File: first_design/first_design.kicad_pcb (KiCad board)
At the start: 2 copper layers, 66 x 57 mm, 0 parts

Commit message: working on PCB design
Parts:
- added 2N7002K1: NMOS_DGS, library_express_pro:SOT23, F.Cu at (147.0, 60.0)
- added 2N7002K2: NMOS_DGS, library_express_pro:SOT23, F.Cu at (159.5, 47.4)
- added AI-1223-TWT-5V-5-R1: Buzzer, library_express_pro:Buzzer_AI-1223-TWT-5V-5-R, F.Cu at (156.5, 32.4)
- added C1: 10uF, library_express_pro:RLC_EIA_3216, F.Cu at (112.0, 62.0)
- added C2: 170uF, library_express_pro:RLC_EIA_3216, F.Cu at (105.7, 62.1)
- added C3: 100nF, library_express_pro:RLC_EIA_3216, F.Cu at (122.3, 48.2)
- added C4: 1uF, library_express_pro:RLC_EIA_3216, F.Cu at (72.0, 70.0)
- added C5: 1uF, library_express_pro:RLC_EIA_3216, F.Cu at (72.0, 75.0)
- added C6: 0.1uF, library_express_pro:RLC_EIA_3216, F.Cu at (60.0, 75.0)
- added C7: 44uF, library_express_pro:RLC_EIA_3216, F.Cu at (66.0, 70.0)
- added C8: 10uF, library_express_pro:RLC_EIA_3216, F.Cu at (106.4, 49.5)
- added C9: 44uF, library_express_pro:RLC_EIA_3216, F.Cu at (61.0, 69.0)
- added J1: Conn_02x20_Odd_Even, library_express_pro:RaspberryPi_pins, F.Cu at (32.8, 27.0)
- added J2: Accelerometer_small, library_express_pro:accelerometer_small, F.Cu at (141.8, 35.2)
- added J3: Accelerometer_standard, library_express_pro:Accelerometer_standard, F.Cu at (100.9, 45.0)
- added J4: Servo_motor, library_express_pro:servo_connector, F.Cu at (114.2, 45.0)
- added L1: 3.3uH, library_express_pro:RLC_EIA_3216, F.Cu at (56.0, 70.0)
- added LDO1: AZ2085, library_express_pro:TO252-2, F.Cu at (135.4, 39.7)
- added MotorConnector1: Conn_01x02, library_express_pro:Connector_pads, F.Cu at (29.0, 72.0)
- added MotorController1: VNH7070BAS, library_express_pro:SO-16N, F.Cu at (41.6, 74.4)
- added None1: IR_LED, library_express_pro:LED_YSL-R531R3D-D2, F.Cu at (143.1, 54.6)
- added Power1: Conn_01x02, library_express_pro:Connector_pads, F.Cu at (85.0, 65.0)
- added R1: 220, library_express_pro:RLC_EIA_3216, F.Cu at (118.8, 52.0)
- added R10: 220, library_express_pro:RLC_EIA_3216, F.Cu at (137.3, 52.0)
- added R11: 82, library_express_pro:RLC_EIA_3216, F.Cu at (131.1, 55.7)
- added R12: 82, library_express_pro:RLC_EIA_3216, F.Cu at (137.3, 55.7)
- added R13: 82, library_express_pro:RLC_EIA_3216, F.Cu at (124.2, 59.5)
- added R14: 82, library_express_pro:RLC_EIA_3216, F.Cu at (130.4, 59.5)
- added R1_buck1: 124k, library_express_pro:RLC_EIA_3216, F.Cu at (66.0, 66.0)
- added R2: 220, library_express_pro:RLC_EIA_3216, F.Cu at (112.6, 53.2)
- added R2_buck1: 22.1K, library_express_pro:RLC_EIA_3216, F.Cu at (72.0, 66.0)
- added R3: 100K, library_express_pro:RLC_EIA_3216, F.Cu at (118.8, 55.7)
- added R4: 10K, library_express_pro:RLC_EIA_3216, F.Cu at (124.9, 55.7)
- added R5: 10K, library_express_pro:RLC_EIA_3216, F.Cu at (118.1, 59.5)
- added R7: 220, library_express_pro:RLC_EIA_3216, F.Cu at (128.5, 48.2)
- added R8: 220, library_express_pro:RLC_EIA_3216, F.Cu at (134.6, 48.2)
- added R9: 220, library_express_pro:RLC_EIA_3216, F.Cu at (131.1, 52.0)
- added R_IR1: 220, library_express_pro:RLC_EIA_3216, F.Cu at (106.5, 53.0)
- added Rmax1: 280, library_express_pro:RLC_EIA_3216, F.Cu at (88.0, 77.0)
- added Si4101DY1: PMOS, library_express_pro:SOT23, F.Cu at (82.0, 77.0)
- added StepDownConverter1: AP65450, library_express_pro:SO-8, F.Cu at (66.0, 75.0)
- added VoltageMonitor1: BD48K60, library_express_pro:SSOP3, F.Cu at (148.9, 50.7)
- added YSL-R531R3D-D1: LED, library_express_pro:LED_YSL-R531R3D-D2, F.Cu at (154.3, 45.8)
- added YSL-R531R3D-D2: LED, library_express_pro:LED_YSL-R531R3D-D2, F.Cu at (160.5, 42.0)
- added YSL-R531R3D-D3: LED, library_express_pro:LED_YSL-R531R3D-D2, F.Cu at (141.8, 60.4)
- added YSL-R531R3D-D4: LED, library_express_pro:LED_YSL-R531R3D-D2, F.Cu at (136.3, 60.4)

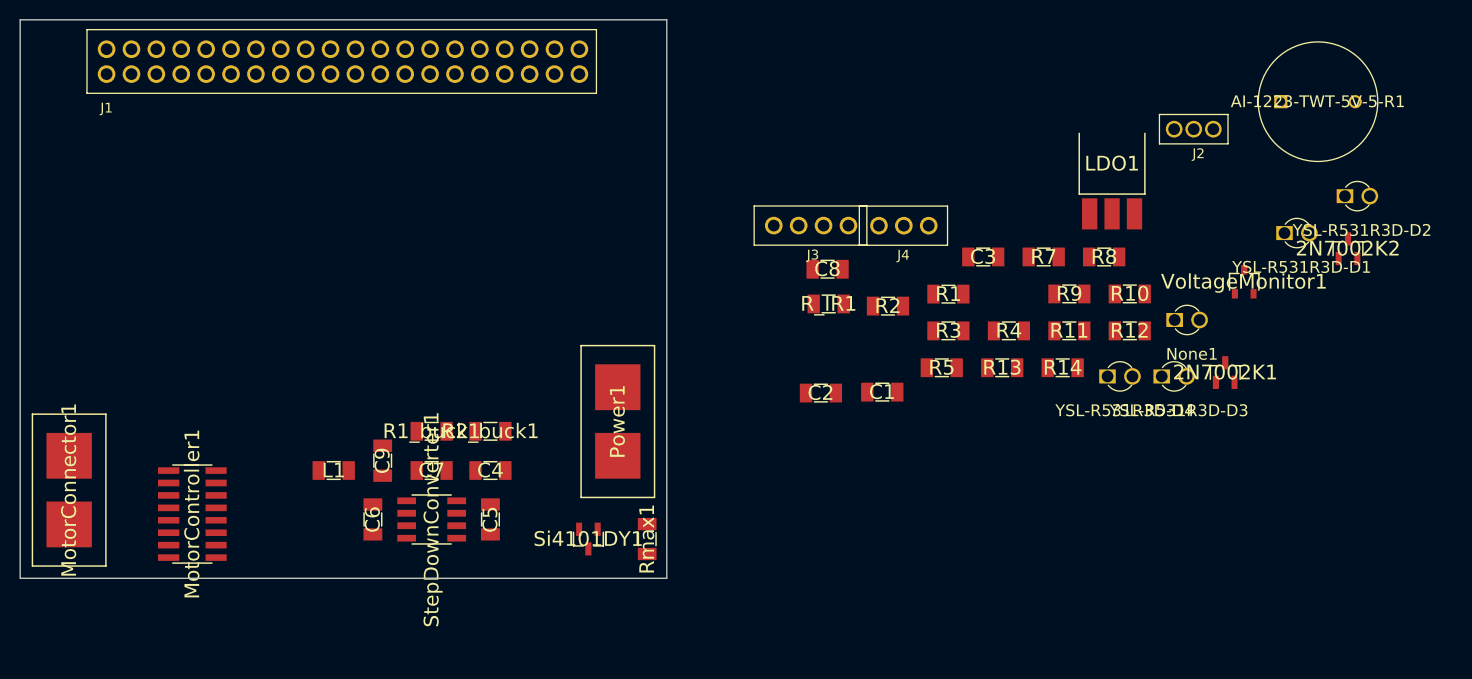
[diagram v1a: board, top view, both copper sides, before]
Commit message: PCB Board first layout
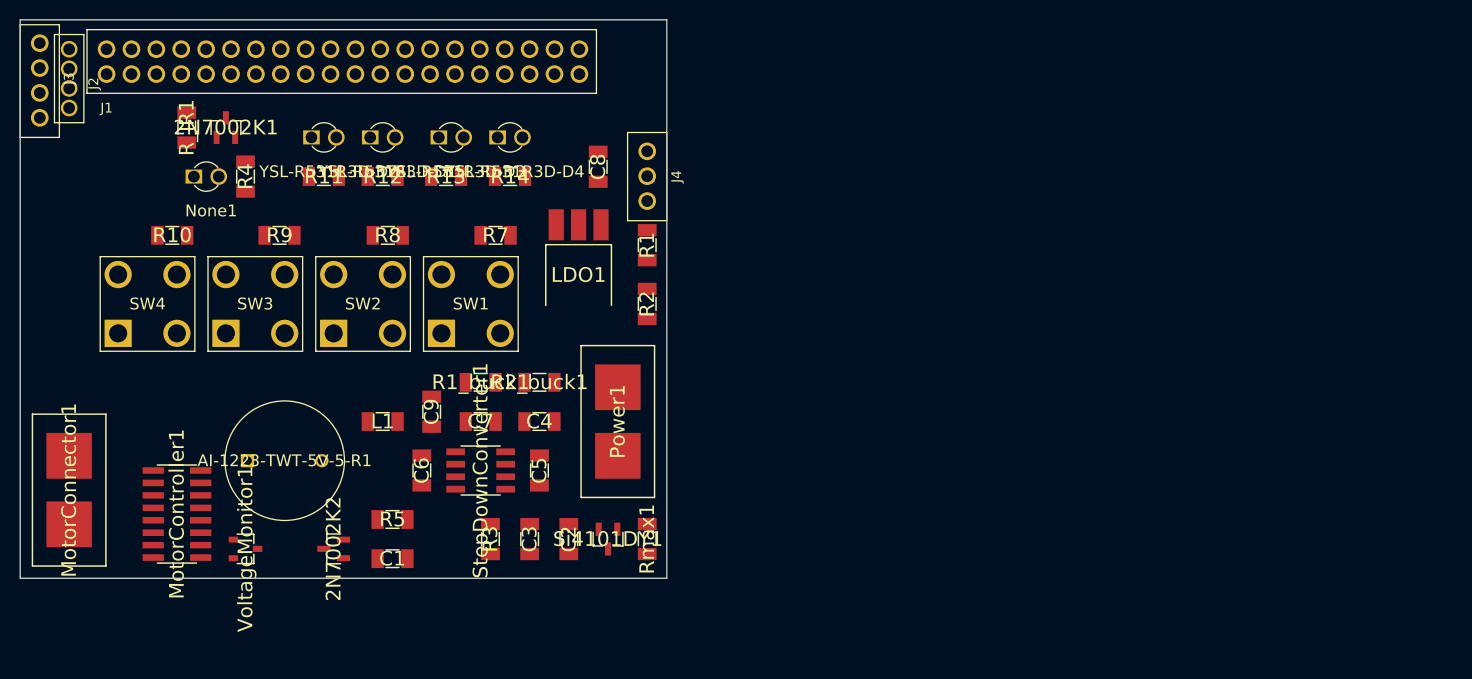
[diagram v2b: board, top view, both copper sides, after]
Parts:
- added SW1: SW_DPST, library_express_pro:button_6x6mm, F.Cu at (67.0, 56.0)
- added SW2: SW_DPST, library_express_pro:button_6x6mm, F.Cu at (56.0, 56.0)
- added SW3: SW_DPST, library_express_pro:button_6x6mm, F.Cu at (45.0, 56.0)
- added SW4: SW_DPST, library_express_pro:button_6x6mm, F.Cu at (34.0, 56.0)
- moved J2 112.8 mm to (29.0, 33.0), turned to 90 degrees
- moved AI-1223-TWT-5V-5-R1 111.7 mm to (51.0, 69.0)
- moved 2N7002K2 108.0 mm to (56.0, 78.0), turned to 90 degrees
- moved YSL-R531R3D-D2 105.7 mm to (55.0, 36.0)
- moved VoltageMonitor1 105.5 mm to (47.0, 78.0), turned to 270 degrees
- moved 2N7002K1 105.0 mm to (45.0, 35.0)
- moved None1 101.2 mm to (43.0, 40.0)
- moved R10 97.9 mm to (39.5, 46.0)
- moved YSL-R531R3D-D1 93.8 mm to (61.0, 36.0)
- moved R9 80.8 mm to (50.5, 46.0)
- moved R4 79.5 mm to (47.0, 40.0), turned to 270 degrees
- moved R12 77.9 mm to (61.0, 40.0)
- moved YSL-R531R3D-D3 77.7 mm to (68.0, 36.0)
- moved R11 77.7 mm to (55.0, 40.0)
- moved J3 75.7 mm to (26.0, 34.0), turned to 90 degrees
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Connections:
- LDO1 pad 1: (no net) -> Net-(LDO1-Pad1)
- LDO1 pad 2: (no net) -> 6V-5V
- LDO1 pad 3: (no net) -> Vbat
- R1 pad 2: Net-(LDO1-Pad~) -> Net-(LDO1-Pad1)
- R2 pad 1: Net-(LDO1-Pad~) -> Net-(LDO1-Pad1)

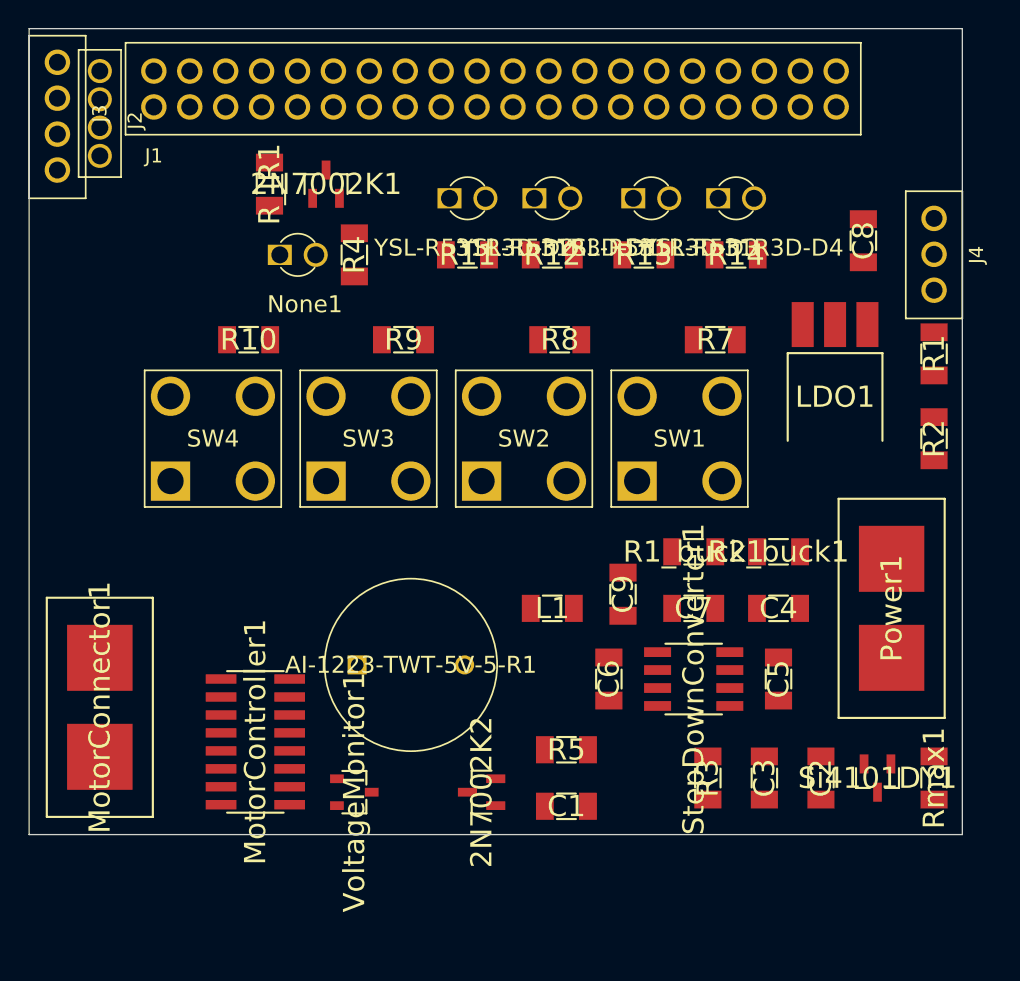
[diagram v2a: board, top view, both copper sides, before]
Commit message: PCB board in the works
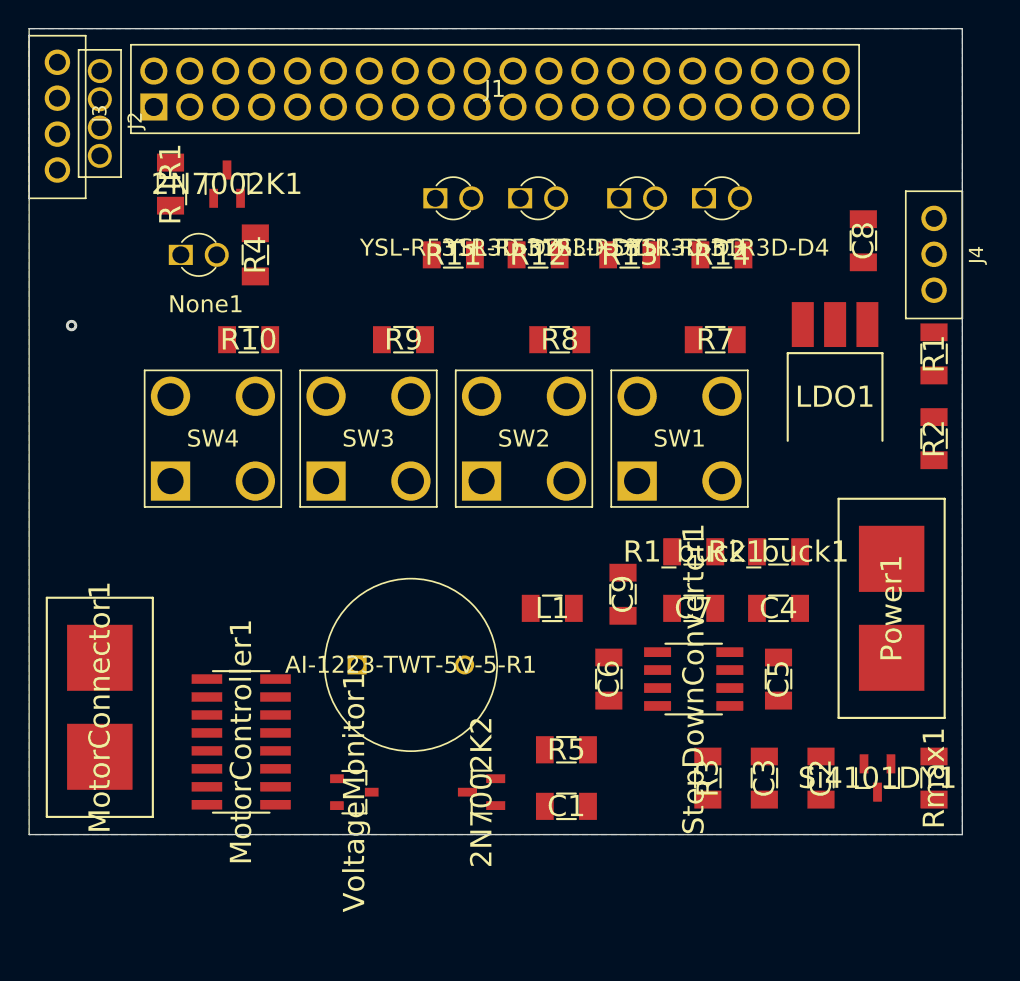
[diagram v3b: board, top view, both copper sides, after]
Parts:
- J1: footprint library_express_pro:RaspberryPi_pins -> library_express_pro:RasPi_header_pro
- moved 2N7002K1 7.00 mm to (38.0, 35.0)
- moved None1 7.00 mm to (36.0, 40.0)
- moved R4 7.00 mm to (40.0, 40.0)
- moved R_IR1 7.00 mm to (34.0, 35.0)
- moved J1 2.54 mm to (32.8, 29.5)
- moved MotorController1 1.00 mm to (39.0, 74.4)
- moved R11 1.00 mm to (54.0, 40.0)
- moved R12 1.00 mm to (60.0, 40.0)
- moved R13 1.00 mm to (66.5, 40.0)
- moved R14 1.00 mm to (73.0, 40.0)
- moved YSL-R531R3D-D1 1.00 mm to (60.0, 36.0)
- moved YSL-R531R3D-D2 1.00 mm to (54.0, 36.0)
- moved YSL-R531R3D-D3 1.00 mm to (67.0, 36.0)
- moved YSL-R531R3D-D4 1.00 mm to (73.0, 36.0)
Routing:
- net GND: vias 0 -> 1
- added copper zone on B.Cu, net GND

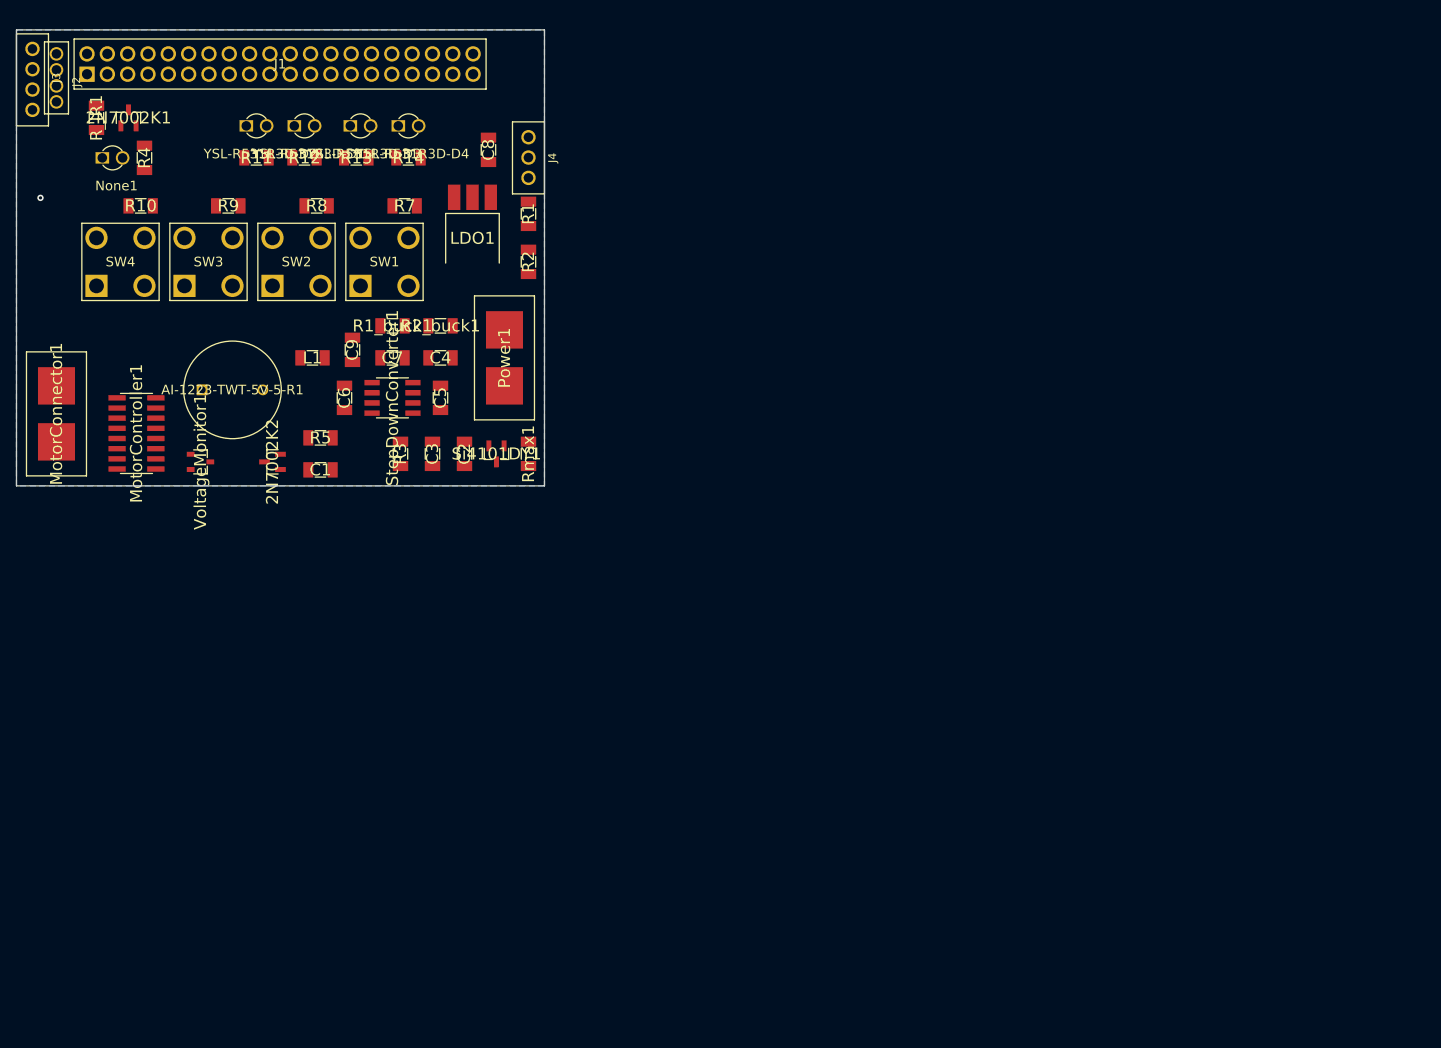
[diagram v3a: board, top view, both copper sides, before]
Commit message: playing with PiHat footprint
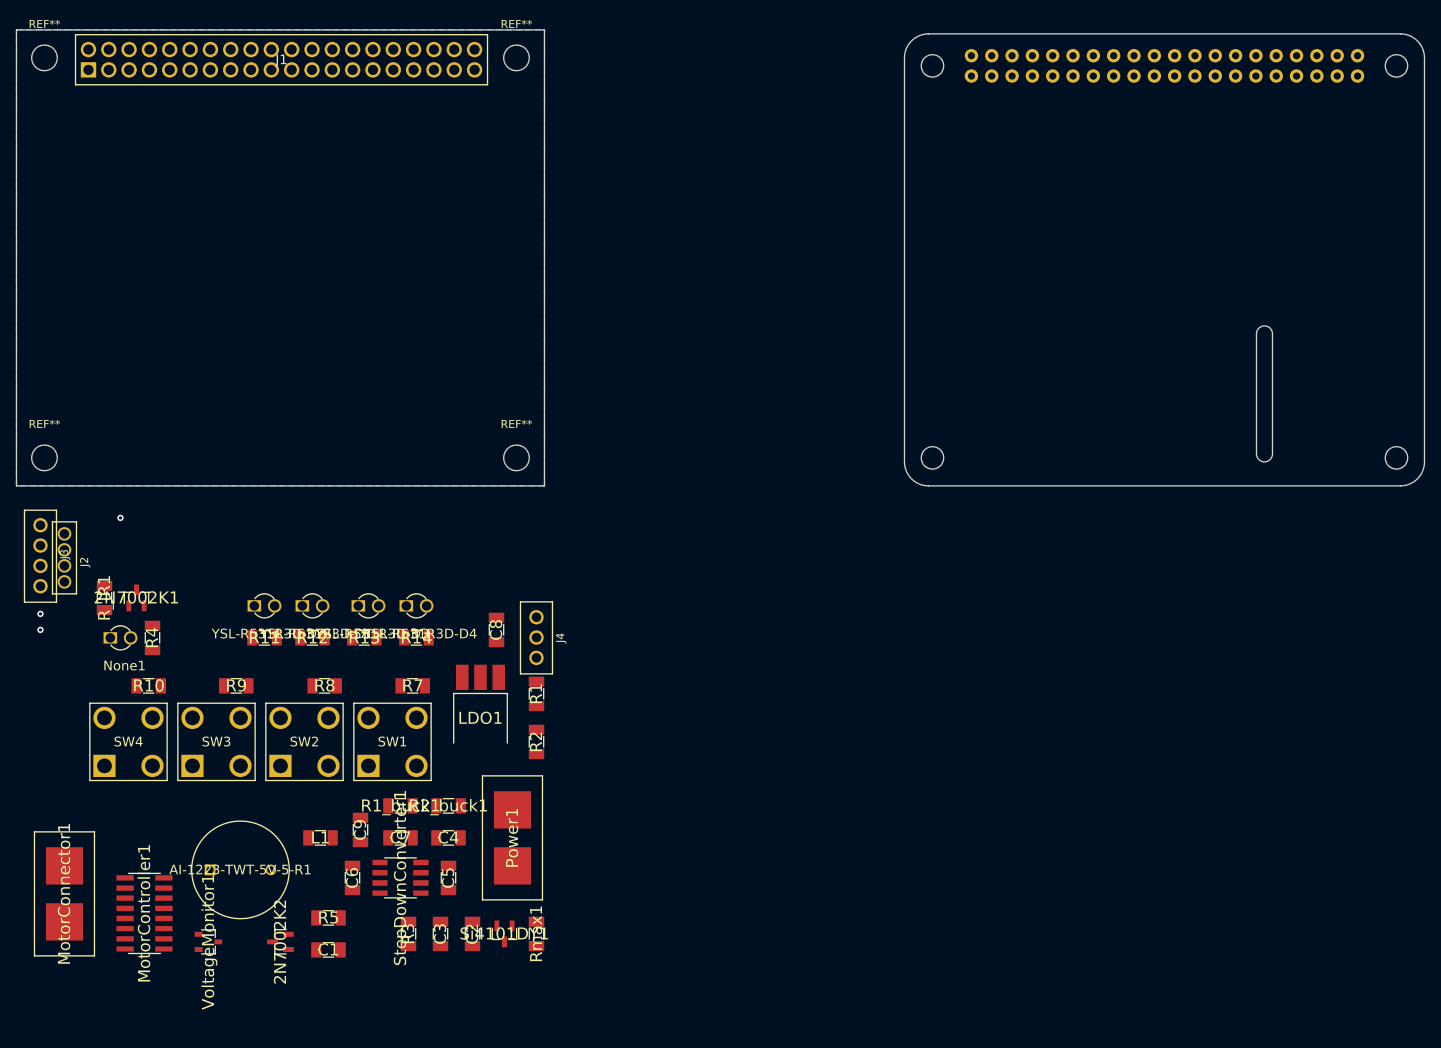
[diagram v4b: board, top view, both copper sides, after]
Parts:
- added REF**: MountingHole_3.2mm_M3, MountingHole:MountingHole_3.2mm_M3, F.Cu at (27.5, 77.5)
- added REF**: MountingHole_3.2mm_M3, MountingHole:MountingHole_3.2mm_M3, F.Cu at (27.5, 27.5)
- added REF**: MountingHole_3.2mm_M3, MountingHole:MountingHole_3.2mm_M3, F.Cu at (86.5, 77.5)
- added REF**: MountingHole_3.2mm_M3, MountingHole:MountingHole_3.2mm_M3, F.Cu at (86.5, 27.5)
- added RPI1: RASPBERRYPI_BPLUS_HATNOSLOTS, Adafruit HaD Proto HAT rev A:PI_HAT_NOSLOTS, F.Cu at (135.0, 81.0)
- moved 2N7002K1 60.0 mm to (39.0, 95.0)
- moved 2N7002K2 60.0 mm to (57.0, 138.0)
- moved AI-1223-TWT-5V-5-R1 60.0 mm to (52.0, 129.0)
- moved C1 60.0 mm to (63.0, 139.0)
- moved C2 60.0 mm to (81.0, 137.0)
- moved C3 60.0 mm to (77.0, 137.0)
- moved C4 60.0 mm to (78.0, 125.0)
- moved C5 60.0 mm to (78.0, 130.0)
- moved C6 60.0 mm to (66.0, 130.0)
- moved C7 60.0 mm to (72.0, 125.0)
- moved C8 60.0 mm to (84.0, 99.0)
- moved C9 60.0 mm to (67.0, 124.0)
- moved J2 60.0 mm to (30.0, 93.0)
- moved J4 60.0 mm to (89.0, 100.0)
- moved L1 60.0 mm to (62.0, 125.0)
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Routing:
- net GND: vias 1 -> 3
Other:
- board size 66 x 57 mm -> 157 x 57 mm
